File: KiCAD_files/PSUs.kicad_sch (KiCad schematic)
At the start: 10 parts

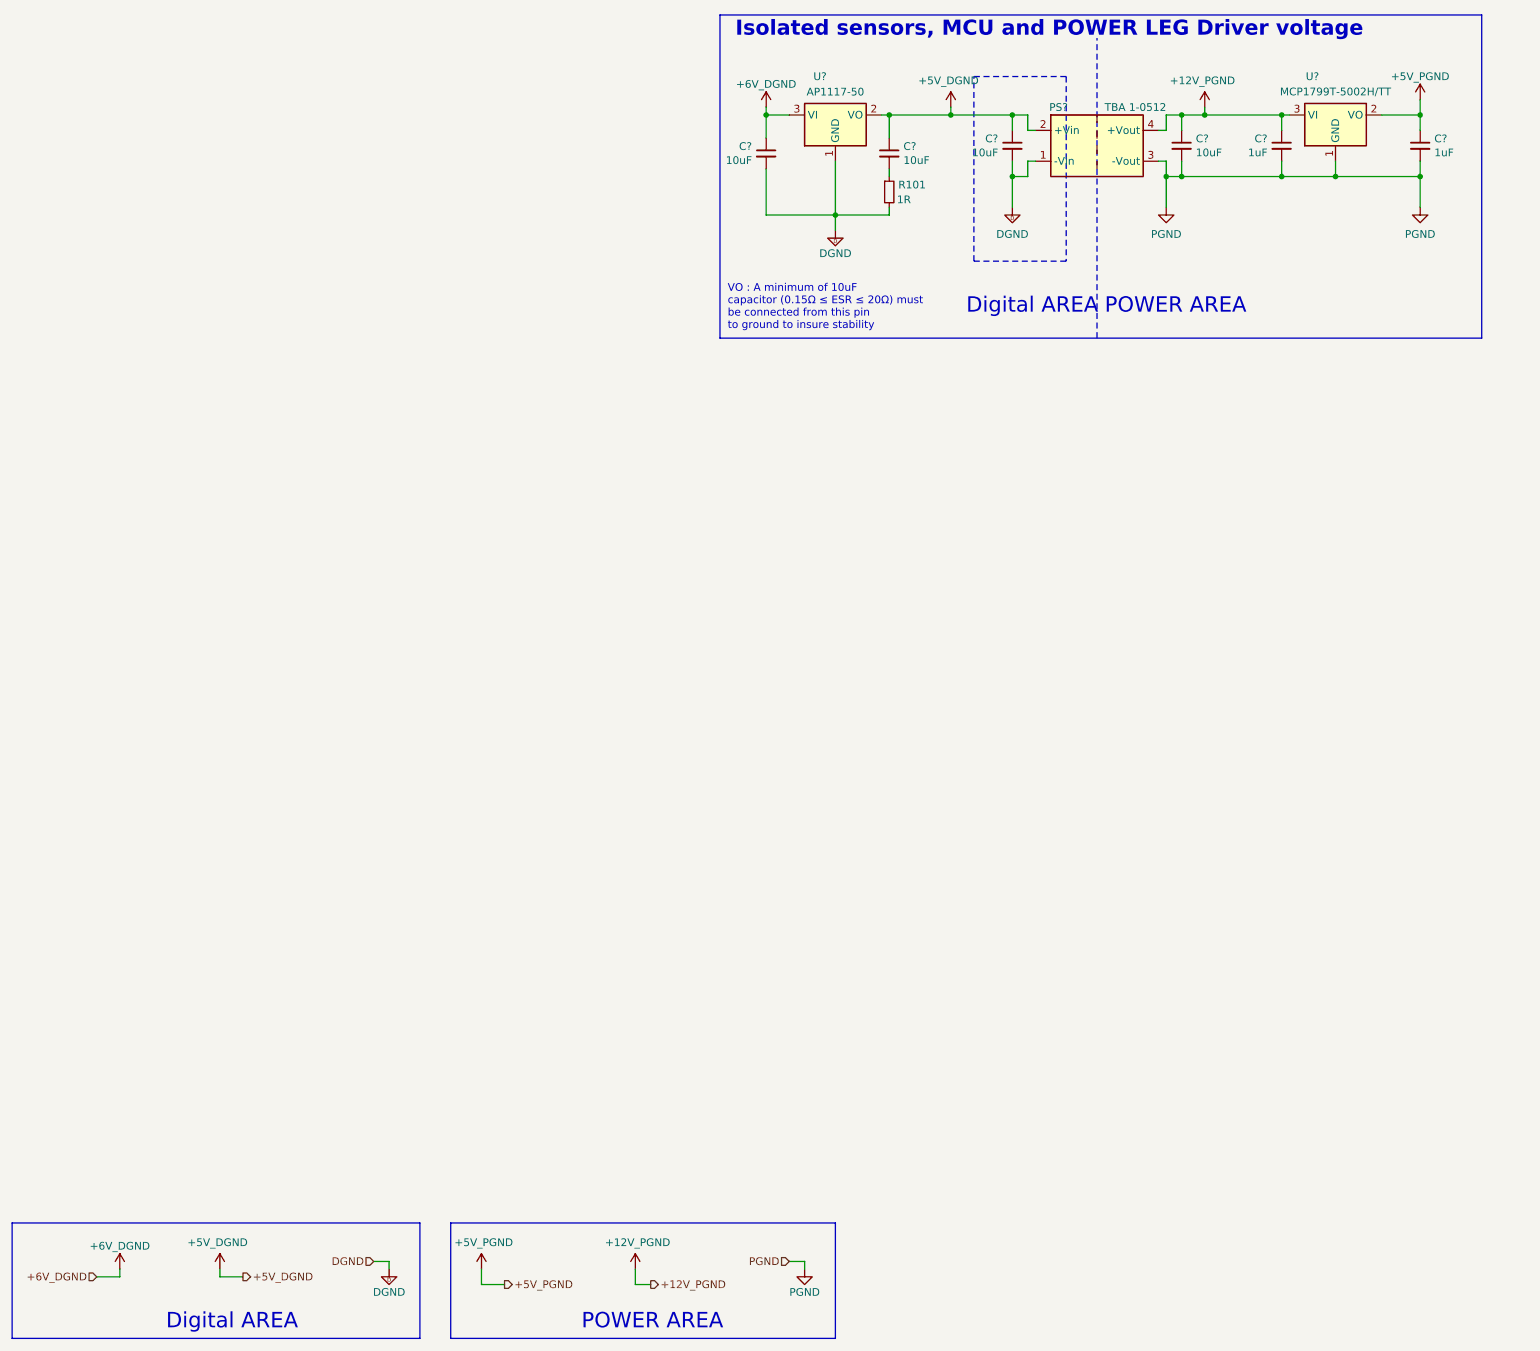
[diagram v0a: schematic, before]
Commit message: removed power ports on hierarchical blocks
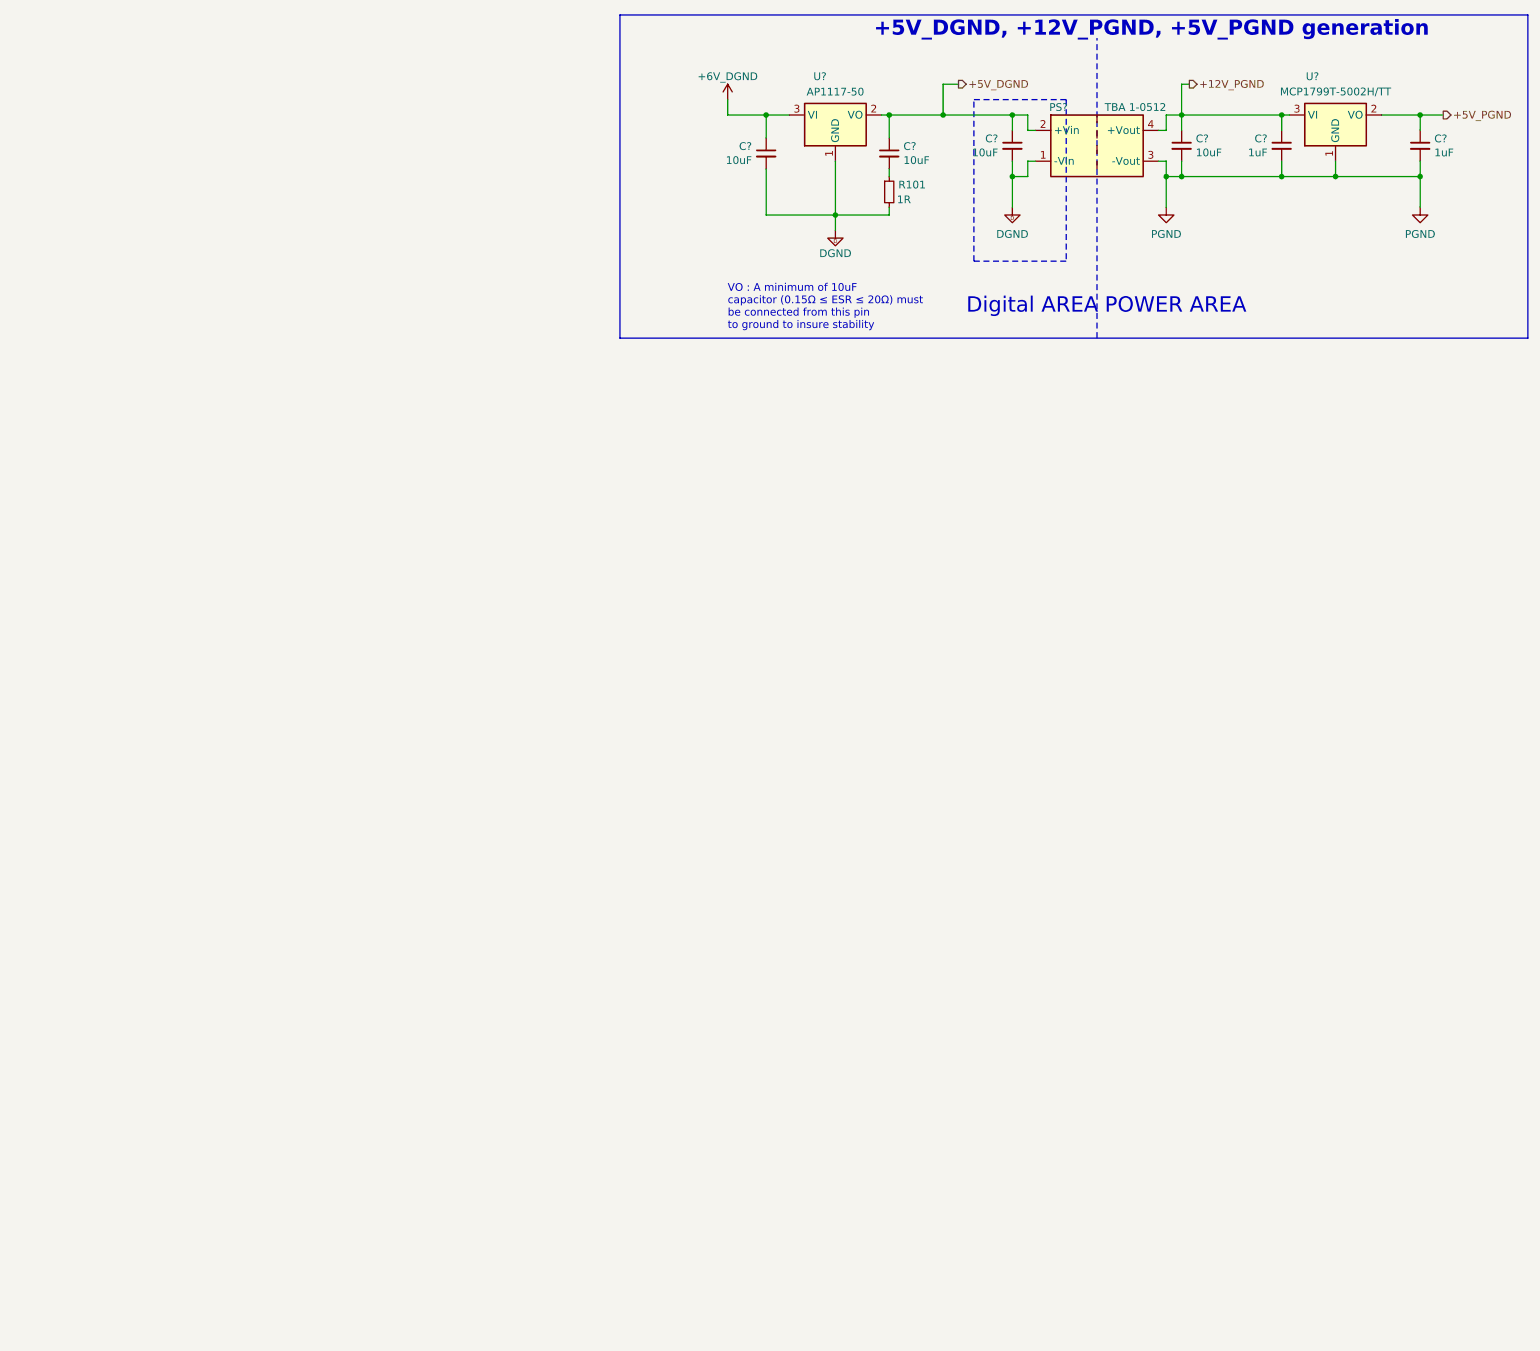
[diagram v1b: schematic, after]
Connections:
- net +12V renamed +12V_PGND
- net +5P renamed +5V_PGND
- net +5VD renamed +5V_DGND
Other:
- note added: "+5V_DGND, +12V_PGND, +5V_PGND generation"
- note removed: "Isolated sensors, MCU and POWER LEG Driver voltage"

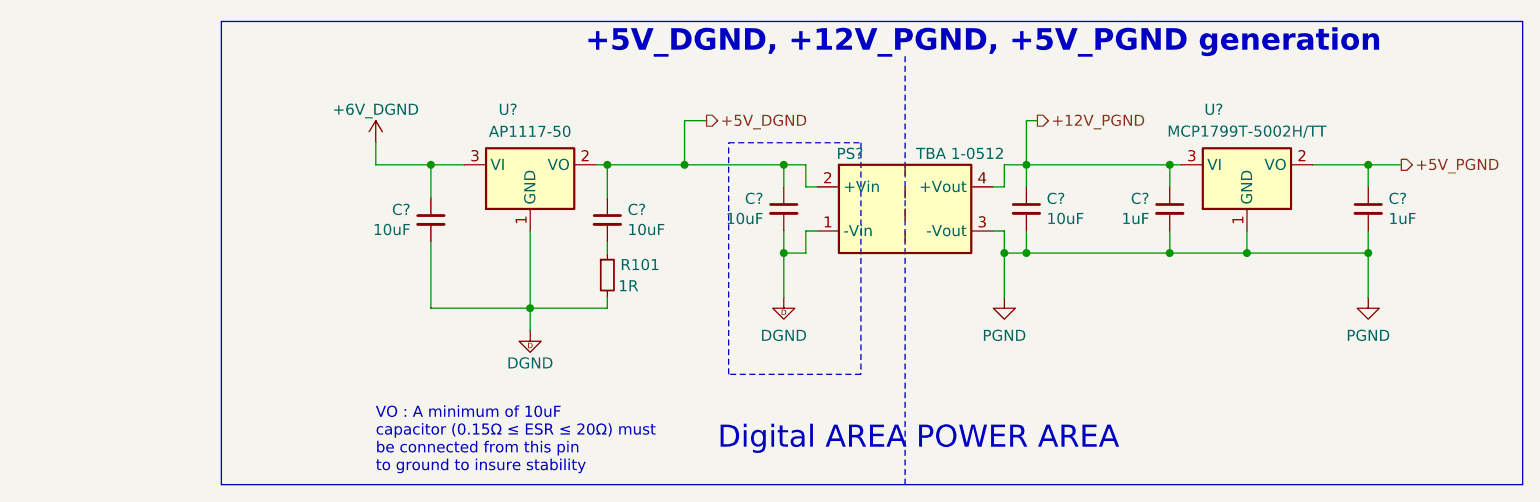
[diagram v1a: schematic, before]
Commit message: full hierarchical sheet
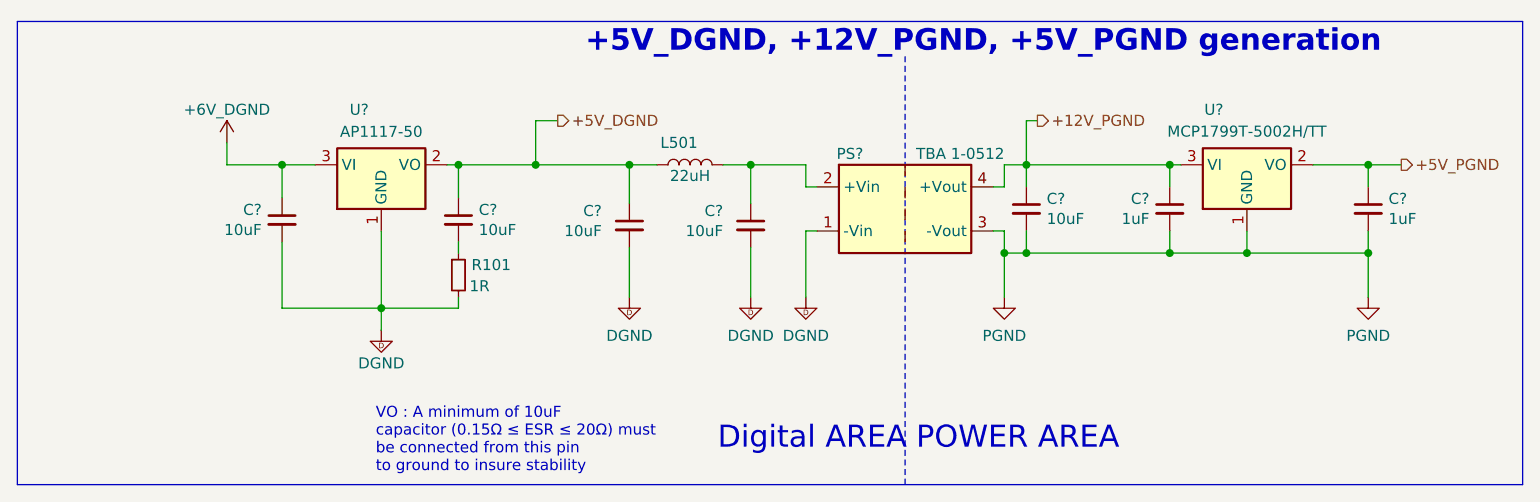
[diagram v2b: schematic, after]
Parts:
- added C?: 10uF, Footprints:C_1210_3225Metric, symbol Device:C_Small
- added L501: 22uH, symbol Device:L
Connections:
- net +5V_DGND: now also L501.1; no longer PS?.2 (+Vin)
- net DGND: now also C?.2
- new net: C?.1, L501.2, PS?.2 (+Vin)
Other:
- moved on the sheet: C?, R101, U?

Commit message: save before starting routing
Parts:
- L?: renamed from L501; footprint (none) -> Inductor_SMD:L_1210_3225Metric; manf# (none) -> CBC3225T220KR
- renumbered R101 to R?
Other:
- title: (none) -> OWNVERTER V0.1
- moved on the sheet: C?, L?, R?, U?

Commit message: dev
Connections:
- net GND renamed PGND
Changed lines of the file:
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@@
     )
   )
-  (symbol (lib_id "power:GND") (at 247.65 93.98 0) (mirror y) (unit 1)
+  (symbol (lib_id "Symbols:PGND") (at 247.65 93.98 0) (mirror y) (unit 1)
     (in_bom yes) (on_board yes) (dnp no) (fields_autoplaced)
     (property "Reference" "#PWR?" (at 247.65 100.33 0)
@@
     )
   )
-  (symbol (lib_id "power:GND") (at 205.74 93.98 0) (mirror y) (unit 1)
+  (symbol (lib_id "Symbols:PGND") (at 205.74 93.98 0) (mirror y) (unit 1)
     (in_bom yes) (on_board yes) (dnp no) (fields_autoplaced)
     (property "Reference" "#PWR?" (at 205.74 100.33 0)

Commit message: Heavy changes on the schematic and on the preliminary routing files
Signed-off-by: Jean Alinei <jean.alinei@laas.fr>
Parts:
- removed C? (x2): 1uF, Footprints:C_0805_2012Metric, symbol Device:C_Small
- removed C? (x5): 10uF, Footprints:C_1210_3225Metric, symbol Device:C_Small
- removed L?: 22uH, Inductor_SMD:L_1210_3225Metric, symbol Device:L
- removed PS?: TBA 1-0512, Footprints:Converter_DCDC_Murata_MEE1SxxxxSC_THT, symbol Converter_DCDC:MEE1S0512SC
- removed R?: 1R, Footprints:R_0805_2012Metric, symbol Device:R_Small
- removed U?: MCP1799T-5002H/TT, Footprints:SOT-23_copy, symbol Regulator_Linear:MCP1754S-5002xCB
- removed U?: AP1117-50, Package_TO_SOT_SMD:SOT-223-3_TabPin2, symbol Regulator_Linear:AP1117-50
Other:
- note removed: "+5V_DGND, +12V_PGND, +5V_PGND generation"
- note removed: "Digital AREA"
- note removed: "POWER AREA"
- note removed: "VO : A minimum of 10uF capacitor (0.15Ω ≤ ESR ≤ 20Ω) must be connected from this pin to ground to insure stability"
